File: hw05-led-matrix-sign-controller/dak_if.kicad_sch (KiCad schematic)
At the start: 9 parts, among them J201 TE 640456-2, J202 TE 640456-4, J203 2x7 Conn to Dak matrix, J204 TE 640456-2, U201 74HC595

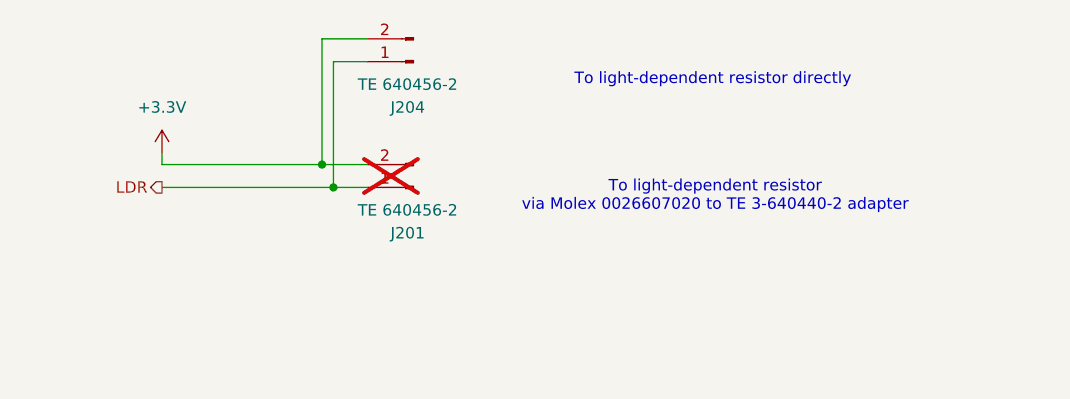
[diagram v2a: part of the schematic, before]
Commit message: Fix part number.
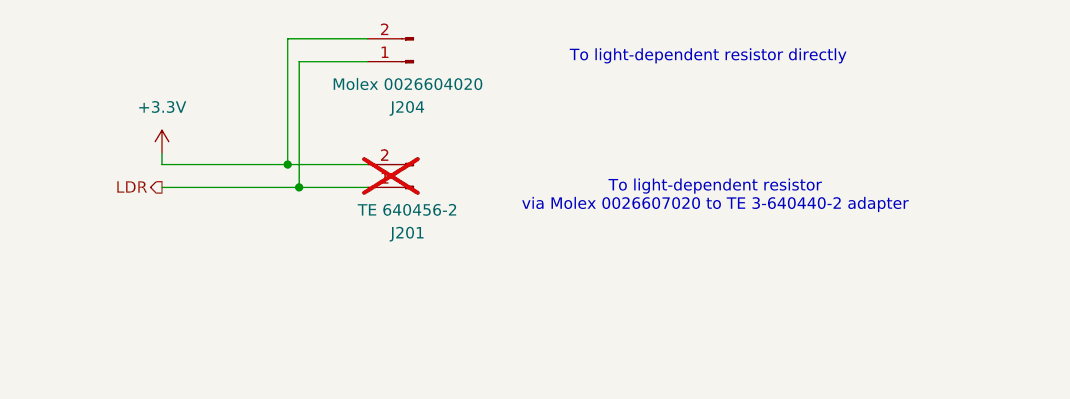
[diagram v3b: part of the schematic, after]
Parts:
- J204: value TE 640456-2 -> Molex 0026604020
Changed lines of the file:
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@@
 		(title "Daktronics-specific circuitry")
 		(date "2025-10-08")
-		(rev "03")
+		(rev "04")
 		(company "Bay Area Electric Railroad Association")
 	)
@@
 	(text "To light-dependent resistor directly"
 		(exclude_from_sim no)
-		(at 202.184 40.132 0)
+		(at 201.676 37.592 0)
 		(effects
 			(font
@@
 	)
 	(junction
-		(at 160.02 52.07)
-		(diameter 0)
-		(color 0 0 0 0)
-	)
-	(junction
 		(at 121.92 116.84)
 		(diameter 0)
@@
 	)
 	(junction
+		(at 154.94 49.53)
+		(diameter 0)
+		(color 0 0 0 0)
+	)
+	(junction
 		(at 242.57 121.92)
+		(diameter 0)
+		(color 0 0 0 0)
+	)
+	(junction
+		(at 156.21 52.07)
 		(diameter 0)
 		(color 0 0 0 0)
@@
 	)
 	(junction
-		(at 158.75 49.53)
-		(diameter 0)
-		(color 0 0 0 0)
-	)
-	(junction
 		(at 193.04 111.76)
 		(diameter 0)
@@
 	(wire
 		(pts
-			(xy 163.83 38.1) (xy 160.02 38.1)
-		)
-		(stroke
-			(width 0)
-			(type default)
-		)
-	)
-	(wire
-		(pts
 			(xy 158.75 116.84) (xy 158.75 111.76)
 		)
@@
 	(wire
 		(pts
-			(xy 160.02 38.1) (xy 160.02 52.07)
-		)
-		(stroke
-			(width 0)
-			(type default)
-		)
-	)
-	(wire
-		(pts
 			(xy 106.68 111.76) (xy 127 111.76)
 		)
@@
 	(wire
 		(pts
-			(xy 160.02 52.07) (xy 163.83 52.07)
+			(xy 140.97 52.07) (xy 156.21 52.07)
 		)
 		(stroke
@@
 	(wire
 		(pts
-			(xy 158.75 49.53) (xy 158.75 35.56)
-		)
-		(stroke
-			(width 0)
-			(type default)
-		)
-	)
-	(wire
-		(pts
 			(xy 166.37 149.86) (xy 121.92 149.86)
 		)
@@
 	(wire
 		(pts
+			(xy 154.94 49.53) (xy 163.83 49.53)
+		)
+		(stroke
+			(width 0)
+			(type default)
+		)
+	)
+	(wire
+		(pts
 			(xy 242.57 144.78) (xy 233.68 144.78)
 		)
@@
 	(wire
 		(pts
-			(xy 158.75 35.56) (xy 163.83 35.56)
-		)
-		(stroke
-			(width 0)
-			(type default)
-		)
-	)
-	(wire
-		(pts
 			(xy 193.04 111.76) (xy 227.33 111.76)
 		)
@@
 	(wire
 		(pts
+			(xy 154.94 35.56) (xy 154.94 49.53)
+		)
+		(stroke
+			(width 0)
+			(type default)
+		)
+	)
+	(wire
+		(pts
 			(xy 149.86 140.97) (xy 156.21 140.97)
 		)
@@
 	(wire
 		(pts
-			(xy 140.97 49.53) (xy 158.75 49.53)
-		)
-		(stroke
-			(width 0)
-			(type default)
-		)
-	)
-	(wire
-		(pts
 			(xy 121.92 116.84) (xy 121.92 149.86)
 		)
@@
 	(wire
 		(pts
-			(xy 158.75 49.53) (xy 163.83 49.53)
+			(xy 140.97 49.53) (xy 154.94 49.53)
 		)
 		(stroke
@@
 	(wire
 		(pts
+			(xy 154.94 35.56) (xy 163.83 35.56)
+		)
+		(stroke
+			(width 0)
+			(type default)
+		)
+	)
+	(wire
+		(pts
 			(xy 147.32 114.3) (xy 157.48 114.3)
 		)
@@
 	(wire
 		(pts
+			(xy 156.21 38.1) (xy 156.21 52.07)
+		)
+		(stroke
+			(width 0)
+			(type default)
+		)
+	)
+	(wire
+		(pts
 			(xy 248.92 137.16) (xy 248.92 139.7)
 		)
@@
 	(wire
 		(pts
-			(xy 140.97 52.07) (xy 160.02 52.07)
-		)
-		(stroke
-			(width 0)
-			(type default)
-		)
-	)
-	(wire
-		(pts
 			(xy 151.13 138.43) (xy 151.13 127)
 		)
@@
 	(wire
 		(pts
+			(xy 156.21 52.07) (xy 163.83 52.07)
+		)
+		(stroke
+			(width 0)
+			(type default)
+		)
+	)
+	(wire
+		(pts
 			(xy 156.21 116.84) (xy 147.32 116.84)
 		)
@@
 		(pts
 			(xy 151.13 127) (xy 147.32 127)
+		)
+		(stroke
+			(width 0)
+			(type default)
+		)
+	)
+	(wire
+		(pts
+			(xy 156.21 38.1) (xy 163.83 38.1)
 		)
 		(stroke
@@
 			)
 		)
-		(property "Value" "TE 640456-2"
+		(property "Value" "Molex 0026604020"
 			(at 168.275 40.64 0)
 			(effects
